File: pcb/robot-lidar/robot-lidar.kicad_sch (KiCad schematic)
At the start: 20 parts, among them J1 AVR-ISP-10, J12 Conn_02x20_Odd_Even, J2 YLIDAR X4, J3 Jack-DC, J5 Conn_01x02, J6 Conn_01x02, U2 LM317-3.3_SOT-223, U2 MPU-6050, U4 MX1508, U6 ATmega328P-A

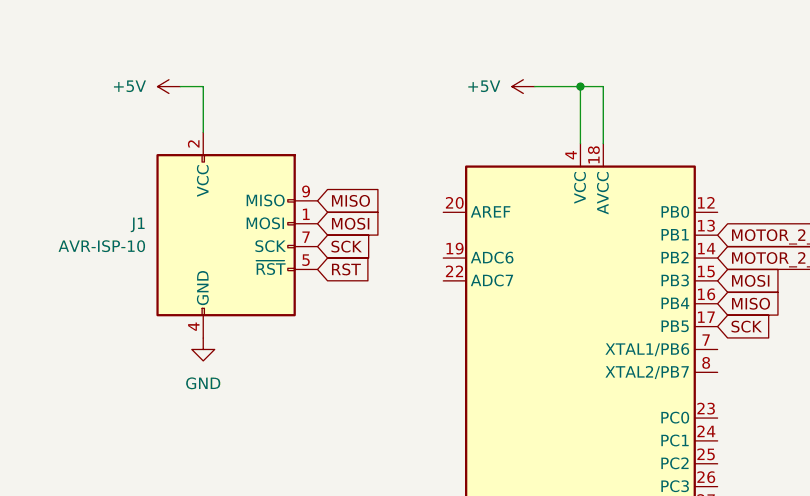
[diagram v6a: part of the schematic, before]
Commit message: wiring atmega and resize board
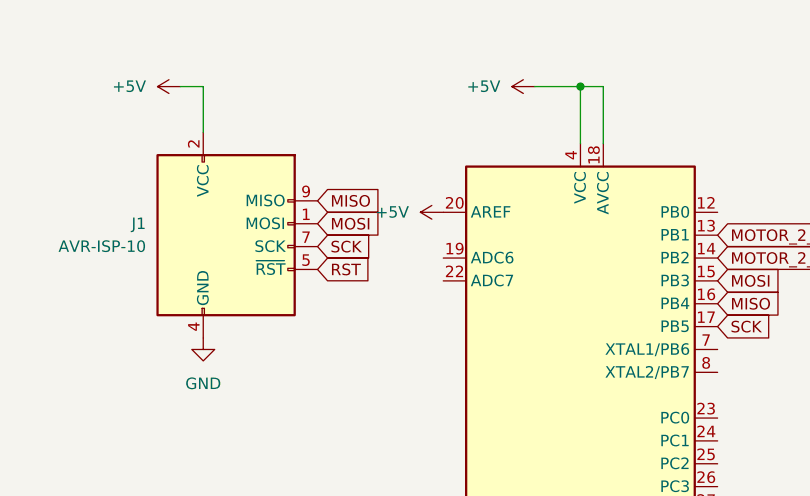
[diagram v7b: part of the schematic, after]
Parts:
- J1: footprint (none) -> Connector_PinSocket_2.54mm:PinSocket_2x05_P2.54mm_Vertical
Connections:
- net +5V: now also U6.20 (AREF)
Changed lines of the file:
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@@
 			)
 		)
-		(property "Footprint" ""
+		(property "Footprint" "Connector_PinSocket_2.54mm:PinSocket_2x05_P2.54mm_Vertical"
 			(at 107.95 39.37 90)
 			(effects
@@
 					(unit 1)
 				)
+			)
+		)
+	)
+	(symbol
+		(lib_id "power:+5V")
+		(at 138.43 36.83 90)
+		(unit 1)
+		(exclude_from_sim no)
+		(in_bom yes)
+		(on_board yes)
+		(dnp no)
+		(fields_autoplaced yes)
+		(property "Reference" "#PWR01"
+			(at 142.24 36.83 0)
+			(effects
+				(font
+					(size 1.27 1.27)
+				)
+				(hide yes)
+			)
+		)
+		(property "Value" "+5V"
+			(at 134.62 36.8299 90)
+			(effects
+				(font
+					(size 1.27 1.27)
+				)
+				(justify left)
+			)
+		)
+		(property "Footprint" ""
+			(at 138.43 36.83 0)
+			(effects
+				(font
+					(size 1.27 1.27)
+				)
+				(hide yes)
+			)
+		)
+		(property "Datasheet" ""
+			(at 138.43 36.83 0)
+			(effects
+				(font
+					(size 1.27 1.27)
+				)
+				(hide yes)
+			)
+		)
+		(property "Description" ""
+			(at 138.43 36.83 0)
+			(effects
+				(font
+					(size 1.27 1.27)
+				)
+				(hide yes)
+			)
+		)
+		(pin "1"
+		)
+		(instances
+			(project "robot-lidar"
+				(path "/cb10bbf7-c2c1-4a0d-8947-ad707931d83b"
+					(reference "#PWR01")
+					(unit 1)
+				)
